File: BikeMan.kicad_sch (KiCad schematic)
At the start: 16 parts, among them J11 PushConnector_8pos, J14 PushConnector_8pos, J3 Conn_01x06_Male, J4 MicroUSB, Q5 DMN62D0U-7, Q6 DMN62D0U-7

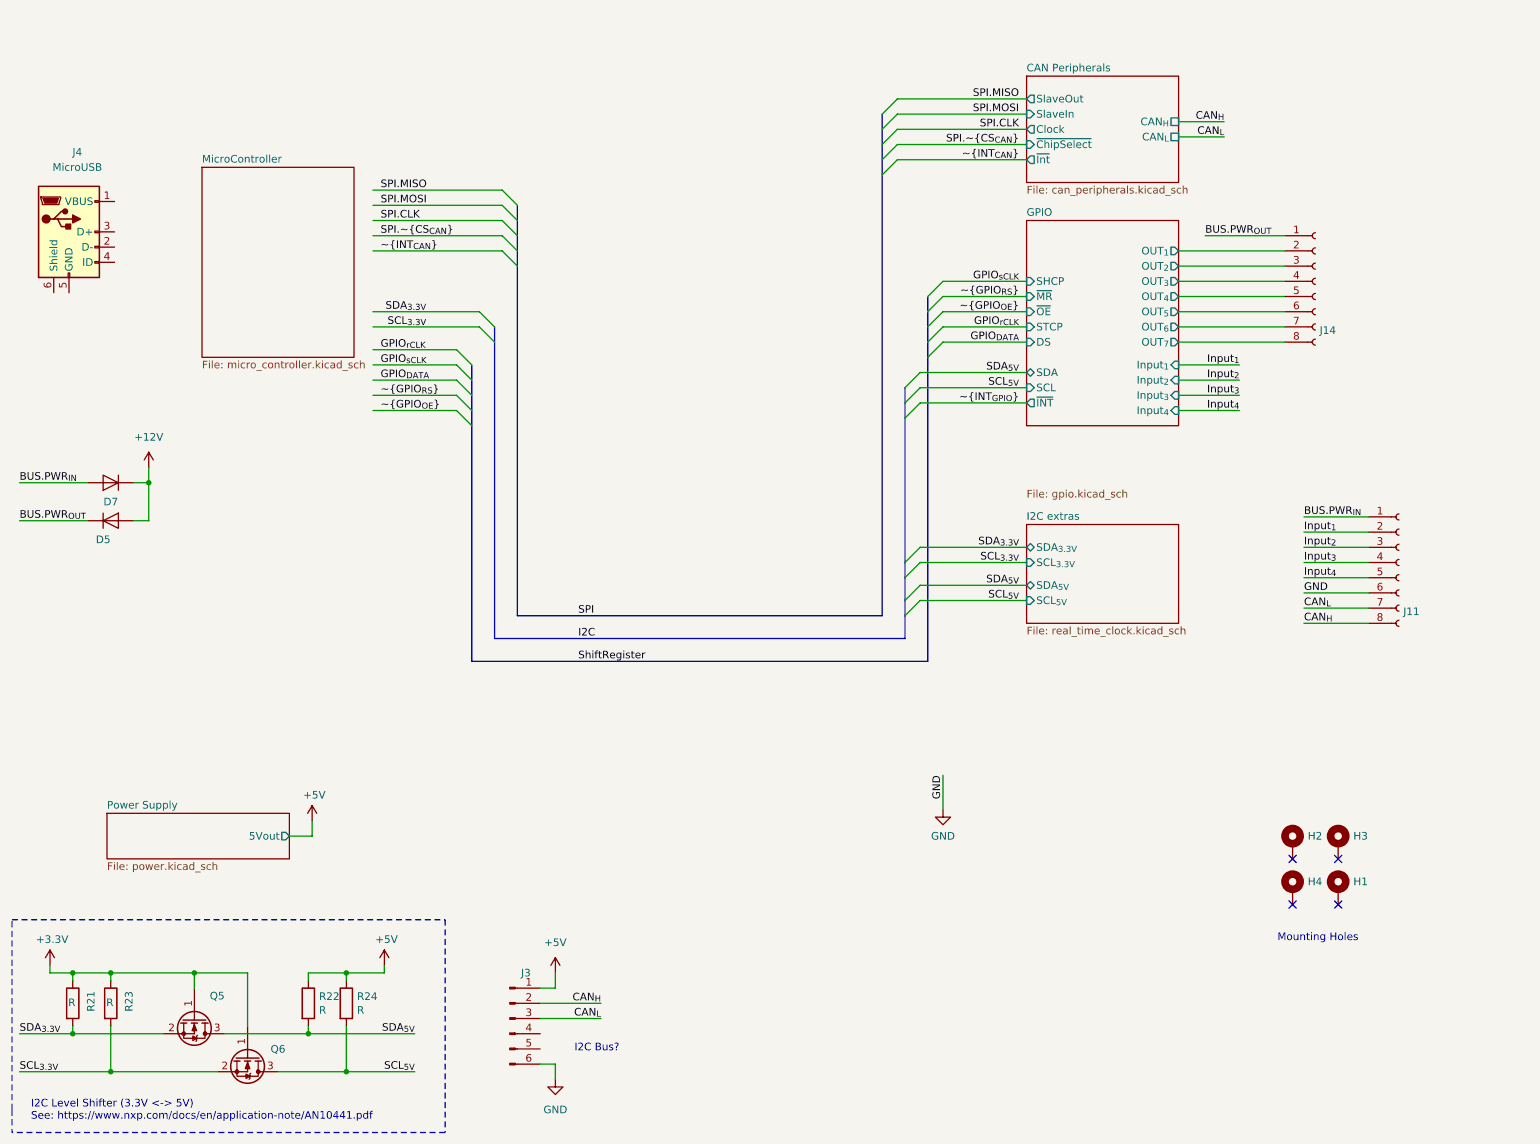
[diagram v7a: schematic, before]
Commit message: components group and placed in roughly the right position
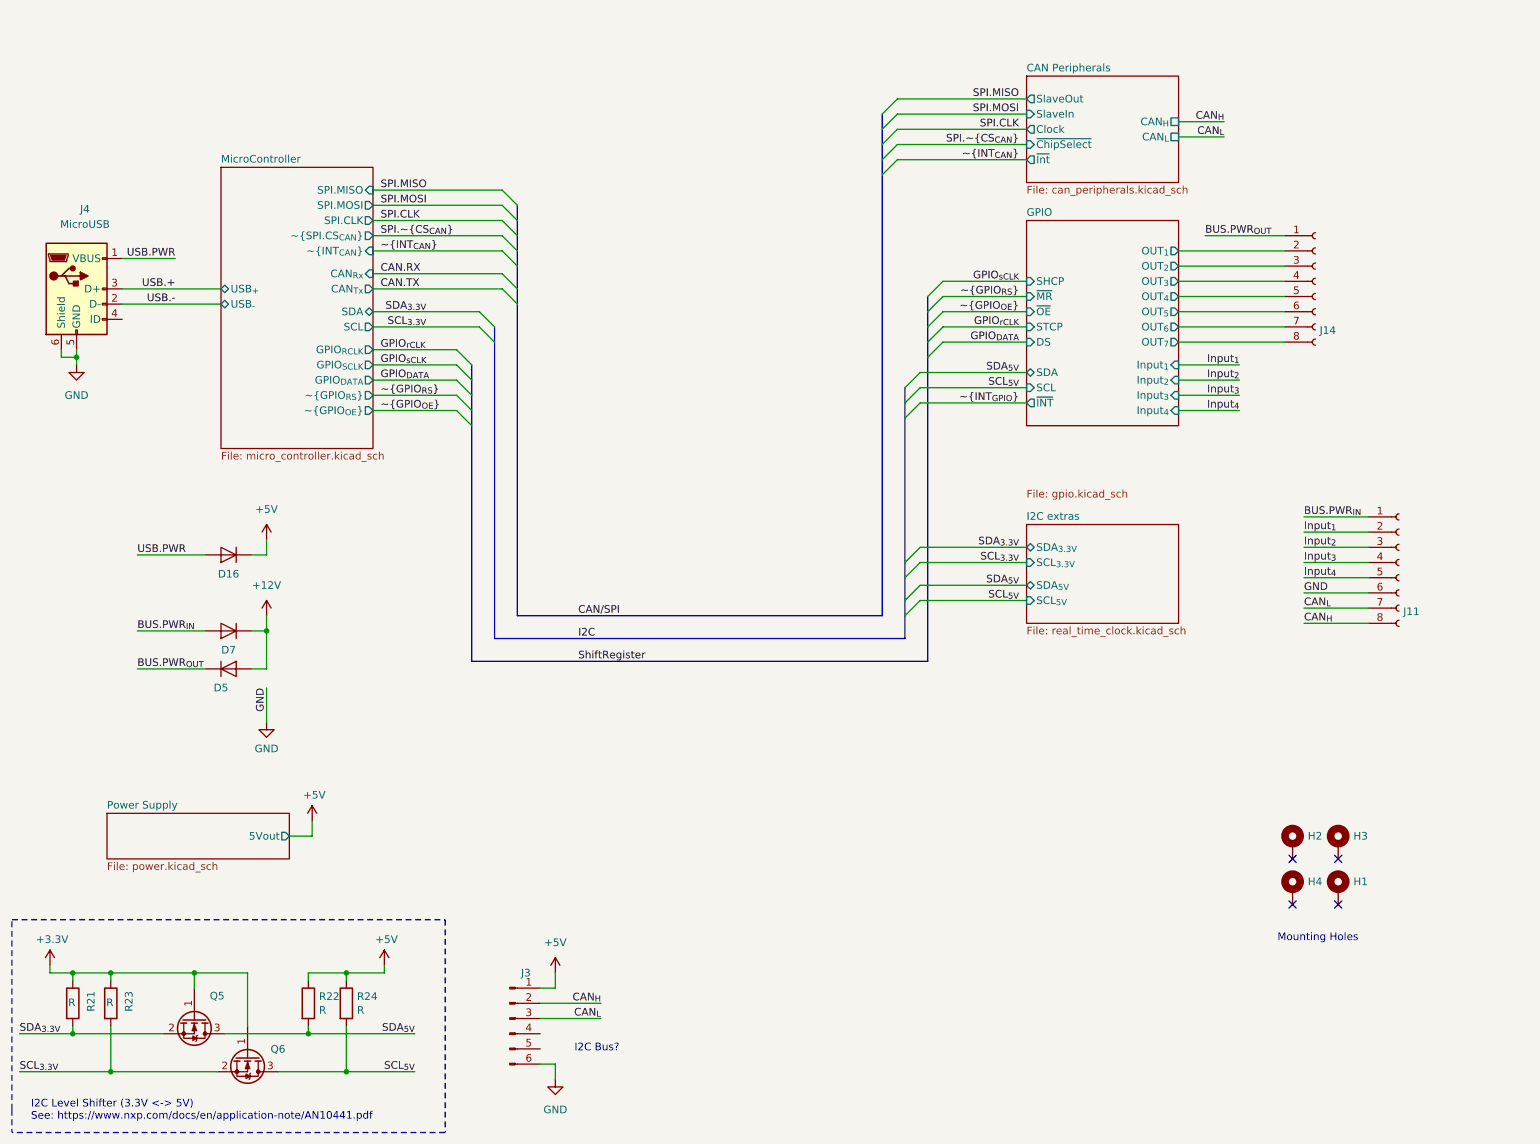
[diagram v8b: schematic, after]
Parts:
- added D16: Diode, Diode_SMD:D_SOD-123F, symbol symbols:Diode
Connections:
- net +5V: now also D16.1 (K)
- net GND: now also J4.5 (GND), J4.6 (Shield)
- net USB.PWR: now reaches J4.1 (VBUS)
- net USB.PWR: now also D16.2 (A)
- net USB.-: now reaches J4.2 (D-)
- net USB.+: now reaches J4.3 (D+)
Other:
- sheet MicroController ports: added CAN_{Rx}, CAN_{Tx}, GPIO_{DATA}, GPIO_{RCLK}, GPIO_{SCLK}, SCL, SDA, SPI.CLK, SPI.MISO, SPI.MOSI, USB_{+}, USB_{-}, ~{GPIO_{OE}}, ~{GPIO_{RS}}, ~{INT_{CAN}}, ~{SPI.CS_{CAN}}; removed none
- moved on the sheet: D5, D7, J4
